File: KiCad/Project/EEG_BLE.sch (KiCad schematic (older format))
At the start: 19 parts, among them P1 ELECTRODES, SW1 PUSH, U1 ADS1299, U2 NRF51822

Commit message: Corrects bias drive resistor value
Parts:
- R1: value 392k -> 1M
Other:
- note added: "Do SRB1 and SRB2 \nneed to be connected \nto something, f.ex: AVSS?"
- note removed: "Do SRB1 and SRB2 \nneed to be connected \nto something, f.ex: AVSS\n(in this bias drive setup)?"
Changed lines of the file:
@@
 P 2450 1650
 F 0 "R1" V 2530 1650 50  0000 C CNN
-F 1 "392k" V 2450 1650 50  0000 C CNN
+F 1 "1M" V 2450 1650 50  0000 C CNN
 F 2 "" V 2380 1650 50  0000 C CNN
 F 3 "" H 2450 1650 50  0000 C CNN
@@
 Can VREFP connect to AVDD \nand VREFN connect to AVSS \nsimply just like here?
 Text Notes 2000 4200 0    43   ~ 0
-Do SRB1 and SRB2 \nneed to be connected \nto something, f.ex: AVSS\n(in this bias drive setup)?
+Do SRB1 and SRB2 \nneed to be connected \nto something, f.ex: AVSS?
 Text Notes 1450 3300 0    39   ~ 0
 Do I need \nRC circuits\non electrodes?

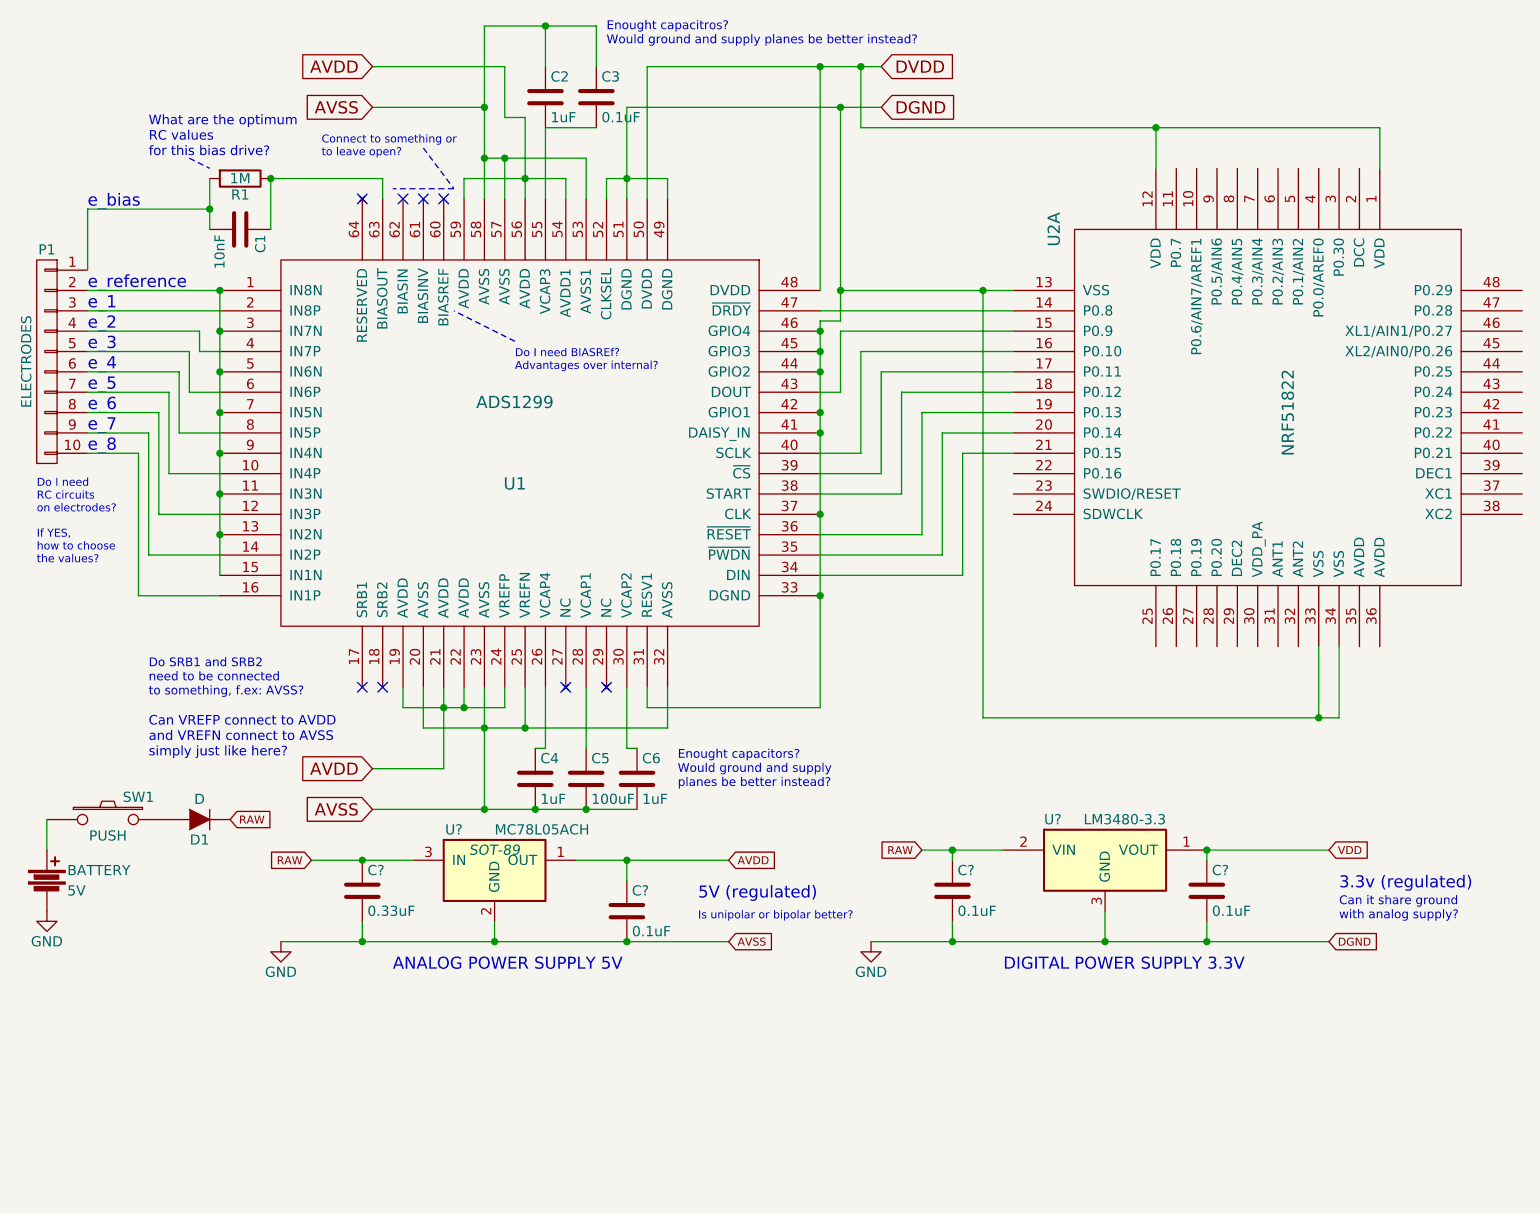
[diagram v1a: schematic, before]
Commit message: Power supply capacitors & VREF connections
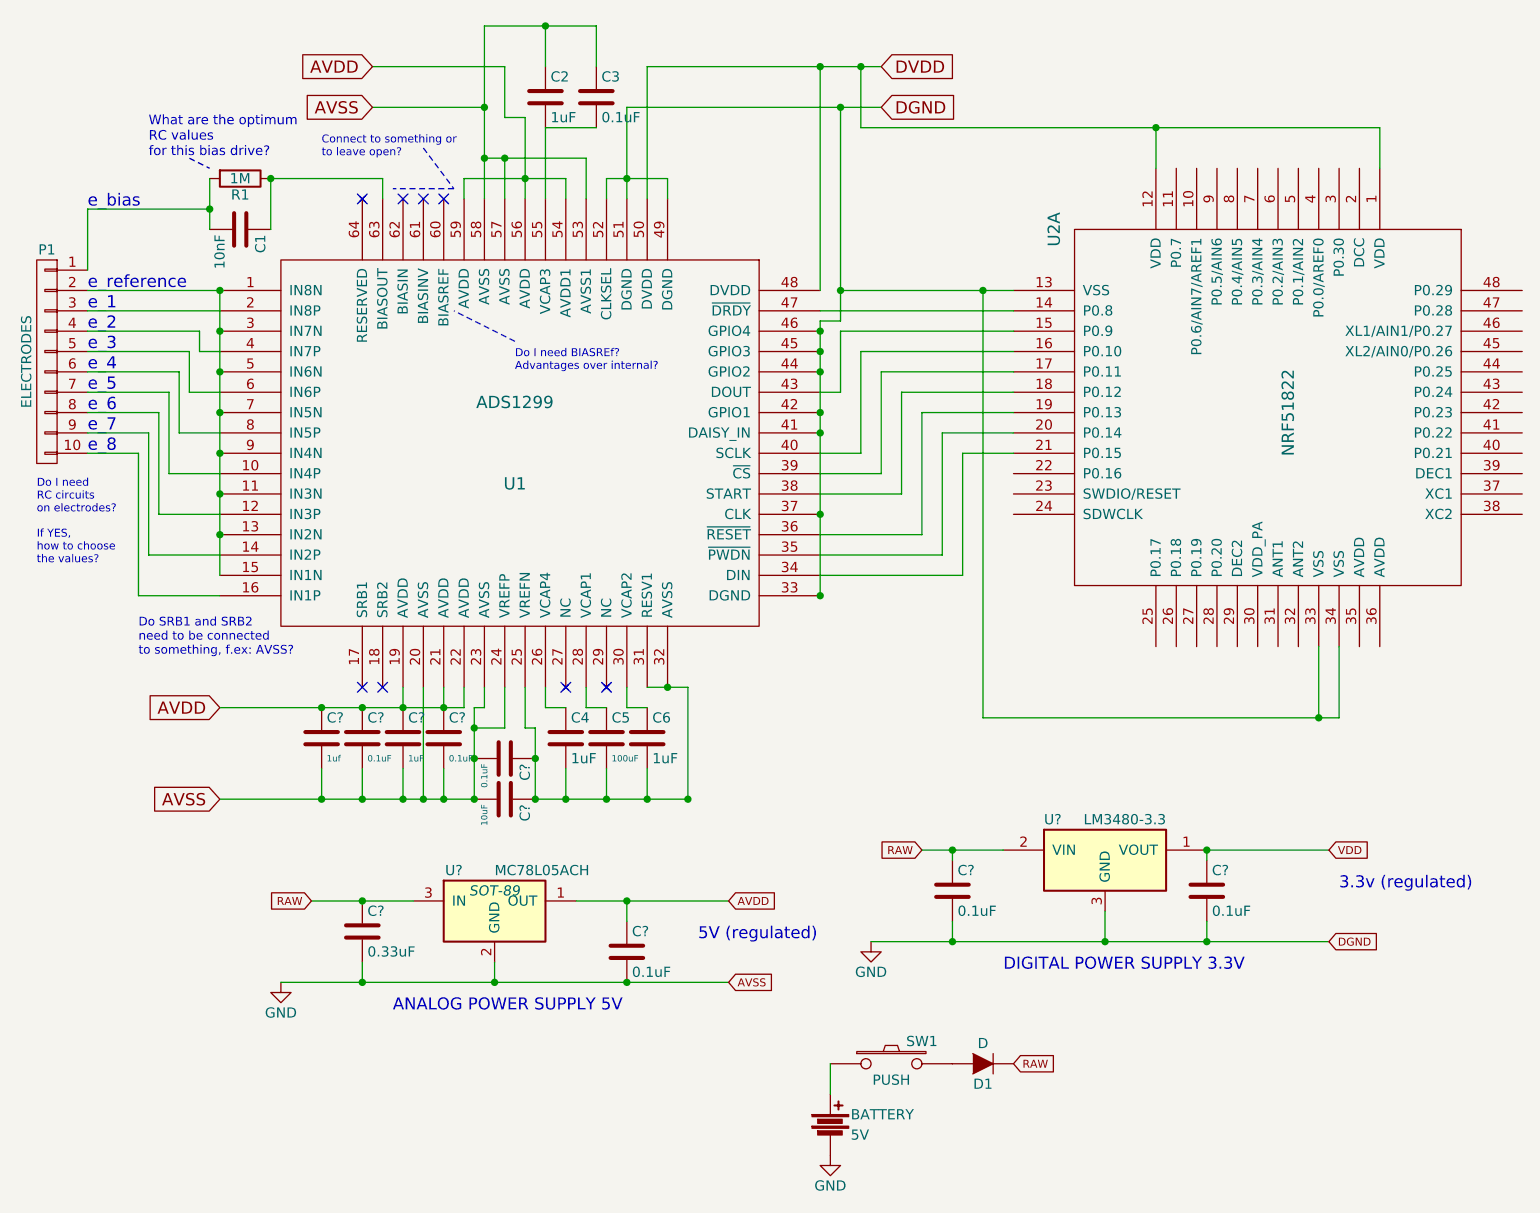
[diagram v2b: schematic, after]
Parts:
- added C?: 10uF, symbol C
- added C? (x3): 0.1uF, symbol C
- added C?: 1uF, symbol C
- added C?: 1uf, symbol C
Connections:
- net AVDD: now also C?.1, C?.1, C?.1, C?.1; no longer U1.24 (VREFP)
- net GND: now also U1.24 (VREFP), C?.2, C?.2, C?.2, C?.2, C?.2, C?.2; no longer C4.2, C5.2, C6.2, U1.25 (VREFN), U1.31 (RESV1), U1.32 (AVSS)
- new net: C4.2, C5.2, C6.2, C?.1, C?.1, U1.25 (VREFN), U1.31 (RESV1), U1.32 (AVSS)
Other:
- note removed: "Can VREFP connect to AVDD \nand VREFN connect to AVSS \nsimply just like here?"
- note removed: "Can it share ground \nwith analog supply?"
- note removed: "Enought capacitors?\nWould ground and supply \nplanes be better instead?"
- note removed: "Enought capacitros?\nWould ground and supply planes be better instead?"
- note removed: "Is unipolar or bipolar better?"
- moved on the sheet: BATTERY, C4, C5, C6, C?, D1, SW1, U?
